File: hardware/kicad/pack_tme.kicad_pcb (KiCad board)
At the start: 2 copper layers, 96 x 90 mm, 132 parts, among them U1 MCP1640T-I/CHY

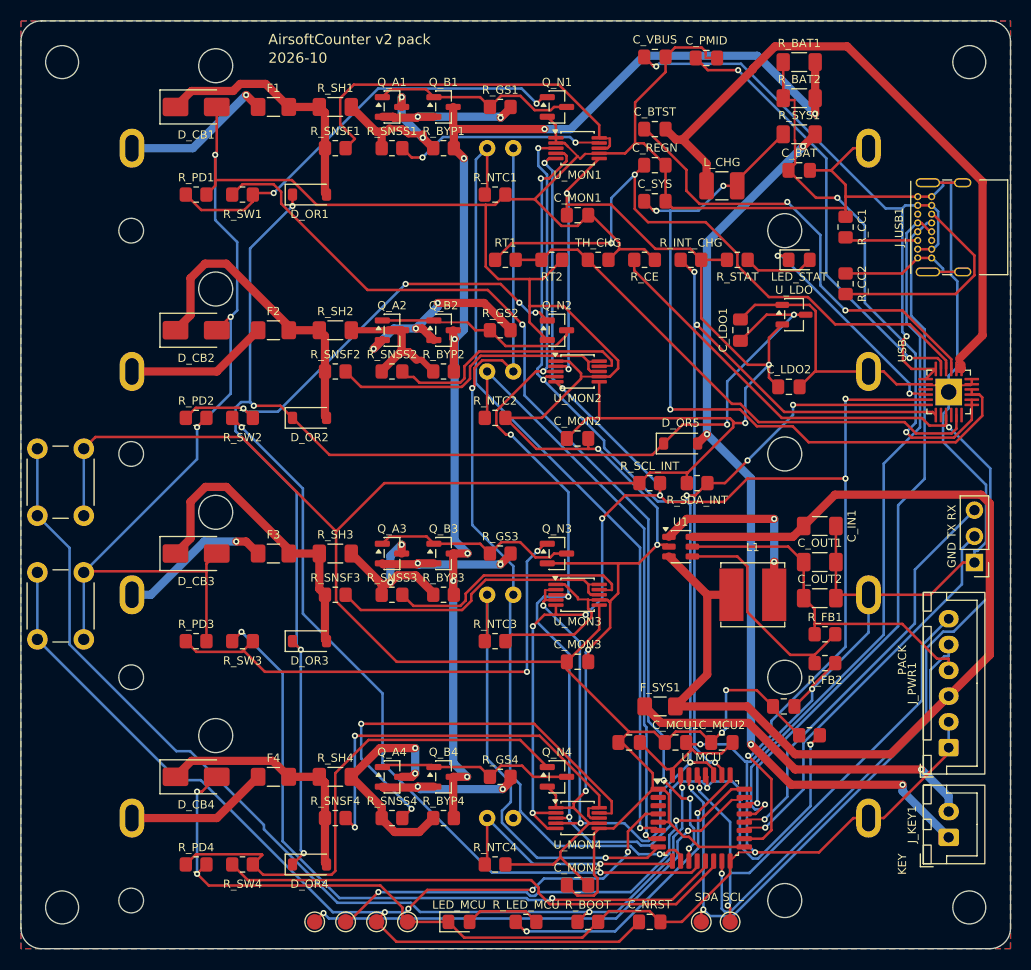
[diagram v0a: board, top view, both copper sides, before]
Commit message: hardware: rebuild every board on KiCad 10.0.7 (fab outputs match the boards)
pack and pack_tme were re-routed by today's generators (the committed copper
was stale); the other boards only pick up a new GND_F zone uuid. Gerbers,
drill, BOM/CPL, schematic PDFs, renders and 1:1 prints regenerated for all 8
boards; ERC/DRC/gerber checks green. pack CPL: J_KEY1 Y follows the fresh
courtyard (-75.75).

Co-Authored-By: Claude Opus 5.5 <noreply@anthropic.com>
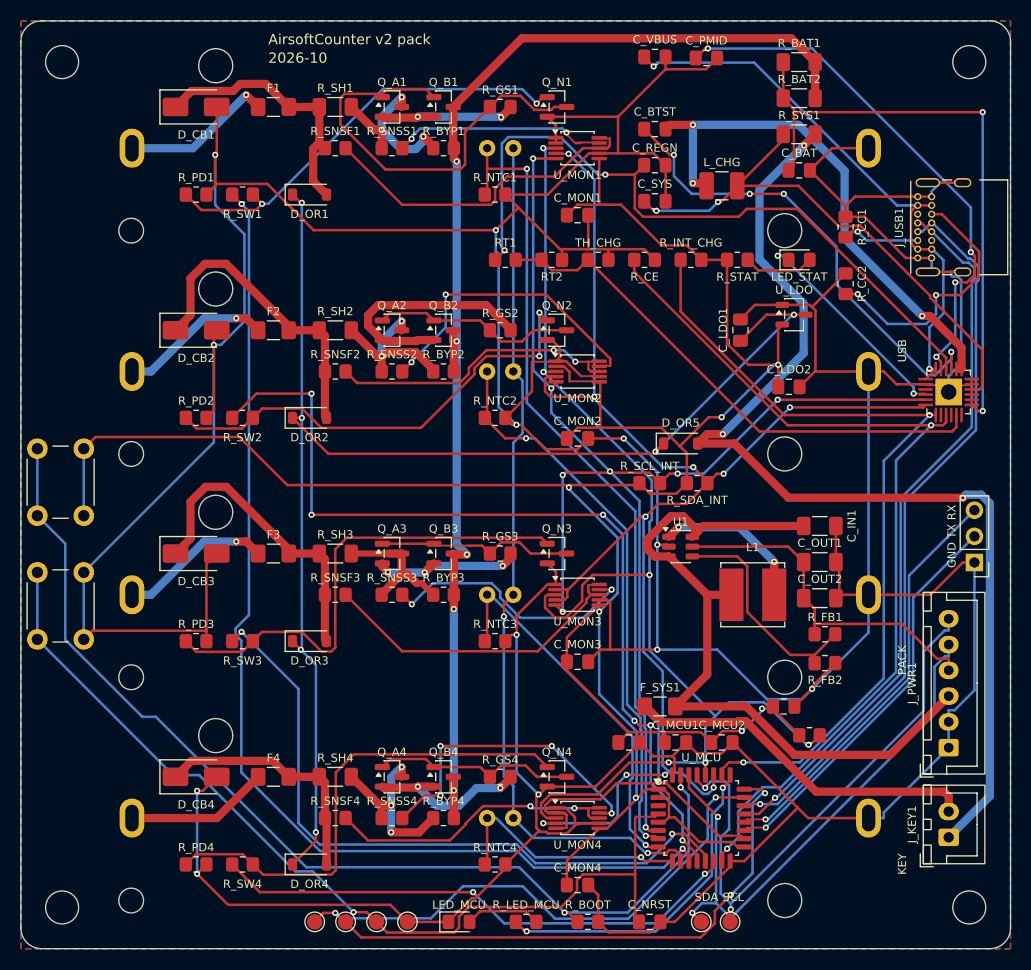
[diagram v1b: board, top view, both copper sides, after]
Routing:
- net +3V3: track 281.8 -> 250.7 mm, vias 6 -> 7
- net VBAT_SW: track 101.7 -> 71.5 mm
- net CELL1_G: track 20.1 -> 41.9 mm
- net SYS_CHG: track 72.6 -> 53.0 mm, vias 3 -> 2
- net NRST: track 111.2 -> 92.5 mm, vias 4 -> 1
- net SYS: track 89.9 -> 104.2 mm, vias 4 -> 3
- net SW_CHG: track 65.5 -> 51.3 mm, vias 0 -> 3
- net CHG_CE: track 104.1 -> 90.1 mm
- net SCL_INT: track 163.5 -> 149.5 mm, vias 10 -> 8
- net SW1_DRV: track 94.5 -> 106.3 mm, vias 4 -> 2
- net SW2_DRV: track 75.2 -> 86.8 mm, vias 2 -> 6
- net SNS_F4: track 40.4 -> 28.9 mm
- net SNS_S4: track 41.3 -> 30.4 mm, vias 2 -> 4
- net VMCU_IN: track 142.5 -> 133.2 mm
- net PMID: track 43.3 -> 51.7 mm, vias 2 -> 4
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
